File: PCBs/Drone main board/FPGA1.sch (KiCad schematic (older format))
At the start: 1 part, among them U1201 10CL040_F484

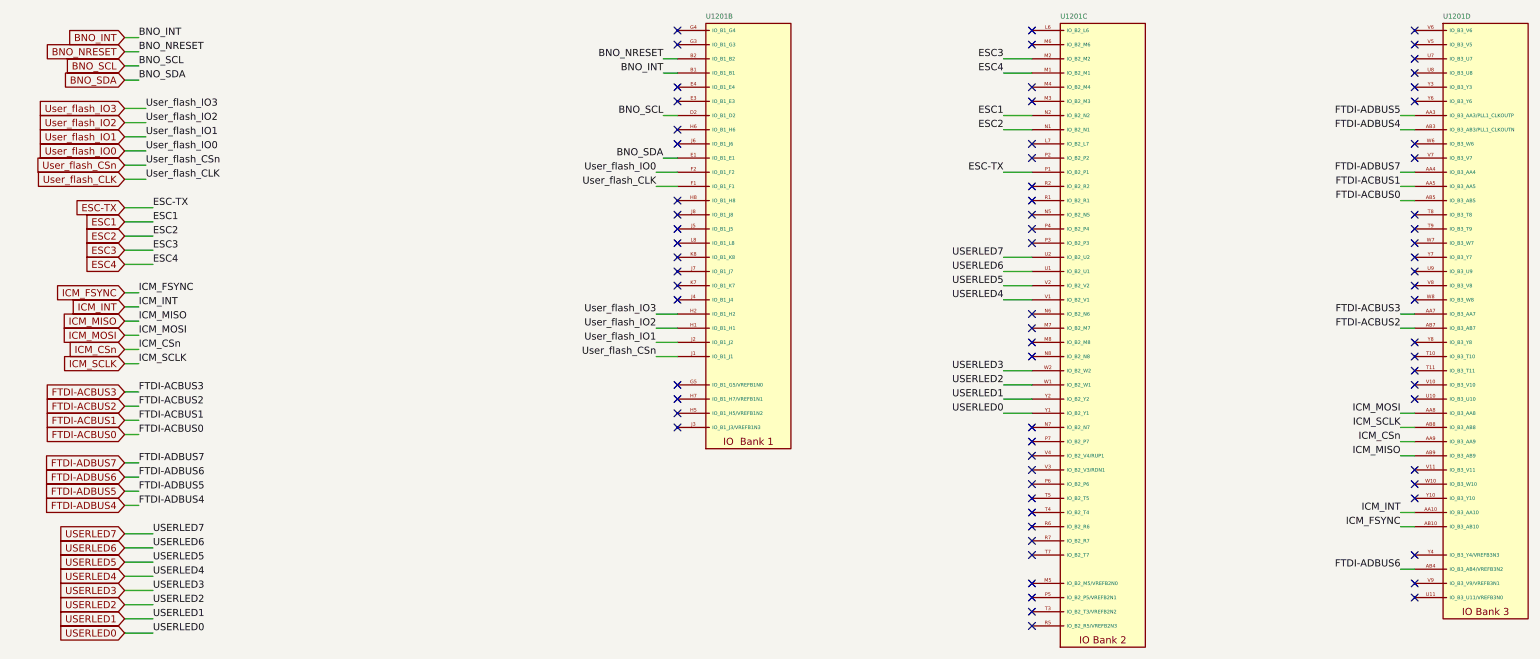
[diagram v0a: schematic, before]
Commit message: Finished (?) the schematic check and update. Next: PCB update
Signed-off-by: Eldalote.Electronics <Eldalote.Electronics@gmail.com>
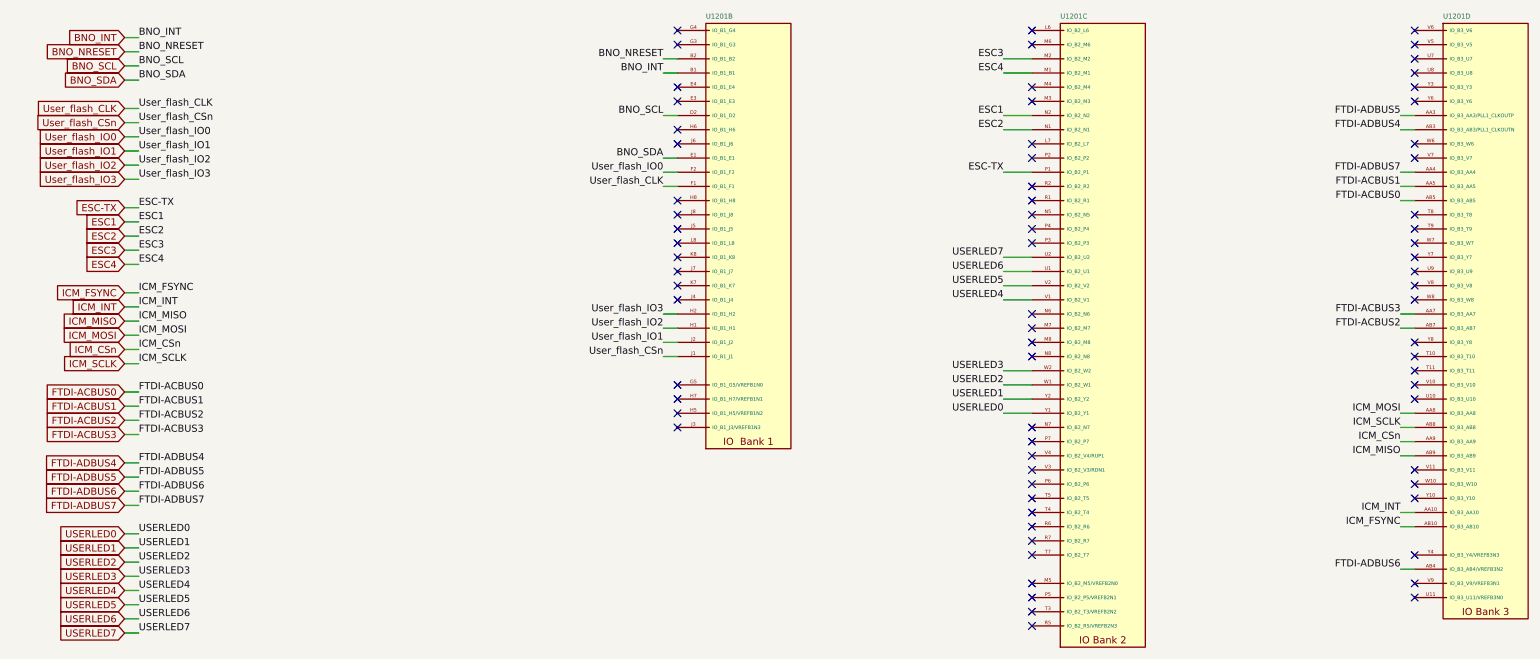
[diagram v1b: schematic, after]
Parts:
- U1201: MfNr (none) -> 10CL040Y
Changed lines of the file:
@@
 F 4 "TRUE" H 6350 -5365 35  0001 L CNN "SPLIT_INST"
 F 5 "(S1+S2+S3+S4+S5+S6+S7+S8+S9+S10+S11+S12+S13)" H 6350 -5410 35  0001 L CNN "SWAP_INFO"
+F 6 "10CL040Y" H 5300 650 50  0001 C CNN "MfNr"
 	2    5300 650
 	1    0    0    -1
@@
 F 4 "TRUE" H 8850 -5365 35  0001 L CNN "SPLIT_INST"
 F 5 "(S1+S2+S3+S4+S5+S6+S7+S8+S9+S10+S11+S12+S13)" H 8850 -5410 35  0001 L CNN "SWAP_INFO"
+F 6 "10CL040Y" H 7800 650 50  0001 C CNN "MfNr"
 	3    7800 650
 	1    0    0    -1
@@
 F 4 "TRUE" H 11550 -5365 35  0001 L CNN "SPLIT_INST"
 F 5 "(S1+S2+S3+S4+S5+S6+S7+S8+S9+S10+S11+S12+S13)" H 11550 -5410 35  0001 L CNN "SWAP_INFO"
+F 6 "10CL040Y" H 10500 650 50  0001 C CNN "MfNr"
 	4    10500 650
 	1    0    0    -1
@@
 Text Label 5000 1000 2    50   ~ 0
 BNO_INT
-Text Label 4950 3000 2    50   ~ 0
+Text Label 5000 3000 2    50   ~ 0
 User_flash_CSn
-Text Label 4950 1700 2    50   ~ 0
+Text Label 5000 1700 2    50   ~ 0
 User_flash_IO0
-Text Label 4950 2900 2    50   ~ 0
+Text Label 5000 2900 2    50   ~ 0
 User_flash_IO1
-Text Label 4950 2800 2    50   ~ 0
+Text Label 5000 2800 2    50   ~ 0
 User_flash_IO2
-Text Label 4950 2700 2    50   ~ 0
+Text Label 5000 2700 2    50   ~ 0
 User_flash_IO3
-Text Label 4950 1800 2    50   ~ 0
+Text Label 5000 1800 2    50   ~ 0
 User_flash_CLK
 Wire Wire Line
-	5100 1800 4950 1800
-Wire Wire Line
-	5100 3000 4950 3000
-Wire Wire Line
-	5100 1700 4950 1700
-Wire Wire Line
-	5100 2900 4950 2900
-Wire Wire Line
-	5100 2800 4950 2800
-Wire Wire Line
-	5100 2700 4950 2700
-Text Label 1350 1650 0    50   ~ 0
+	5100 1800 5000 1800
+Wire Wire Line
+	5100 3000 5000 3000
+Wire Wire Line
+	5100 1700 5000 1700
+Wire Wire Line
+	5100 2900 5000 2900
+Wire Wire Line
+	5100 2800 5000 2800
+Wire Wire Line
+	5100 2700 5000 2700
+Text Label 1300 1350 0    50   ~ 0
 User_flash_CSn
-Text Label 1350 1550 0    50   ~ 0
+Text Label 1300 1450 0    50   ~ 0
 User_flash_IO0
-Text Label 1350 1450 0    50   ~ 0
+Text Label 1300 1550 0    50   ~ 0
 User_flash_IO1
-Text Label 1350 1350 0    50   ~ 0
+Text Label 1300 1650 0    50   ~ 0
 User_flash_IO2
-Text Label 1350 1250 0    50   ~ 0
+Text Label 1300 1750 0    50   ~ 0
 User_flash_IO3
-Text Label 1350 1750 0    50   ~ 0
+Text Label 1300 1250 0    50   ~ 0
 User_flash_CLK
+Text GLabel 1200 1250 0    50   Input ~ 0
+User_flash_CLK
+Text GLabel 1200 1350 0    50   Input ~ 0
+User_flash_CSn
+Text GLabel 1200 1450 0    50   Input ~ 0
+User_flash_IO0
+Text GLabel 1200 1550 0    50   Input ~ 0
+User_flash_IO1
+Text GLabel 1200 1650 0    50   Input ~ 0
+User_flash_IO2
 Text GLabel 1200 1750 0    50   Input ~ 0
-User_flash_CLK
-Text GLabel 1200 1650 0    50   Input ~ 0
-User_flash_CSn
-Text GLabel 1200 1550 0    50   Input ~ 0
-User_flash_IO0
-Text GLabel 1200 1450 0    50   Input ~ 0
-User_flash_IO1
-Text GLabel 1200 1350 0    50   Input ~ 0
-User_flash_IO2
-Text GLabel 1200 1250 0    50   Input ~ 0
 User_flash_IO3
 Wire Wire Line
-	1200 1750 1350 1750
-Wire Wire Line
-	1200 1650 1350 1650
-Wire Wire Line
-	1200 1550 1350 1550
-Wire Wire Line
-	1200 1450 1350 1450
-Wire Wire Line
-	1200 1350 1350 1350
-Wire Wire Line
-	1200 1250 1350 1250
+	1200 1250 1300 1250
+Wire Wire Line
+	1200 1350 1300 1350
+Wire Wire Line
+	1200 1450 1300 1450
+Wire Wire Line
+	1200 1550 1300 1550
+Wire Wire Line
+	1200 1650 1300 1650
+Wire Wire Line
+	1200 1750 1300 1750
 Text GLabel 1200 2350 0    50   Input ~ 0
 ESC4
@@
 ESC-TX
 Wire Wire Line
-	1200 1950 1400 1950
-Text Label 1400 1950 0    50   ~ 0
+	1200 1950 1300 1950
+Text Label 1300 1950 0    50   ~ 0
 ESC-TX
-Text Label 1400 2050 0    50   ~ 0
+Text Label 1300 2050 0    50   ~ 0
 ESC1
-Text Label 1400 2150 0    50   ~ 0
+Text Label 1300 2150 0    50   ~ 0
 ESC2
-Text Label 1400 2250 0    50   ~ 0
+Text Label 1300 2250 0    50   ~ 0
 ESC3
-Text Label 1400 2350 0    50   ~ 0
+Text Label 1300 2350 0    50   ~ 0
 ESC4
 Wire Wire Line
-	1200 2050 1400 2050
-Wire Wire Line
-	1200 2150 1400 2150
-Wire Wire Line
-	1200 2250 1400 2250
-Wire Wire Line
-	1200 2350 1400 2350
+	1200 2050 1300 2050
+Wire Wire Line
+	1200 2150 1300 2150
+Wire Wire Line
+	1200 2250 1300 2250
+Wire Wire Line
+	1200 2350 1300 2350
 Wire Wire Line
 	7600 1700 7400 1700
@@
 Text Label 10200 4200 2    50   ~ 0
 ICM_FSYNC
+Text Label 1300 3750 0    50   ~ 0
+FTDI-ADBUS4
+Text Label 1300 3850 0    50   ~ 0
+FTDI-ADBUS5
+Text Label 1300 3950 0    50   ~ 0
+FTDI-ADBUS6
 Text Label 1300 4050 0    50   ~ 0
+FTDI-ADBUS7
+Text Label 1300 3250 0    50   ~ 0
+FTDI-ACBUS0
+Text Label 1300 3350 0    50   ~ 0
+FTDI-ACBUS1
+Text Label 1300 3450 0    50   ~ 0
+FTDI-ACBUS2
+Text Label 1300 3550 0    50   ~ 0
+FTDI-ACBUS3
+Wire Wire Line
+	1300 3750 1200 3750
+Wire Wire Line
+	1300 3850 1200 3850
+Wire Wire Line
+	1300 3950 1200 3950
+Wire Wire Line
+	1300 4050 1200 4050
+Wire Wire Line
+	1300 3250 1200 3250
+Wire Wire Line
+	1300 3350 1200 3350
+Wire Wire Line
+	1300 3450 1200 3450
+Wire Wire Line
+	1300 3550 1200 3550
+Text GLabel 1200 3750 0    50   Input ~ 0
 FTDI-ADBUS4
-Text Label 1300 3950 0    50   ~ 0
+Text GLabel 1200 3850 0    50   Input ~ 0
 FTDI-ADBUS5
-Text Label 1300 3850 0    50   ~ 0
+Text GLabel 1200 3950 0    50   Input ~ 0
 FTDI-ADBUS6
-Text Label 1300 3750 0    50   ~ 0
+Text GLabel 1200 4050 0    50   Input ~ 0
 FTDI-ADBUS7
-Text Label 1300 3550 0    50   ~ 0
+Text GLabel 1200 3250 0    50   Input ~ 0
 FTDI-ACBUS0
-Text Label 1300 3450 0    50   ~ 0
+Text GLabel 1200 3350 0    50   Input ~ 0
 FTDI-ACBUS1
-Text Label 1300 3350 0    50   ~ 0
+Text GLabel 1200 3450 0    50   Input ~ 0
 FTDI-ACBUS2
-Text Label 1300 3250 0    50   ~ 0
-FTDI-ACBUS3
-Wire Wire Line
-	1300 4050 1200 4050
-Wire Wire Line
-	1300 3950 1200 3950
-Wire Wire Line
-	1300 3850 1200 3850
-Wire Wire Line
-	1300 3750 1200 3750
-Wire Wire Line
-	1300 3550 1200 3550
-Wire Wire Line
-	1300 3450 1200 3450
-Wire Wire Line
-	1300 3350 1200 3350
-Wire Wire Line
-	1300 3250 1200 3250
-Text GLabel 1200 4050 0    50   Input ~ 0
-FTDI-ADBUS4
-Text GLabel 1200 3950 0    50   Input ~ 0
-FTDI-ADBUS5
-Text GLabel 1200 3850 0    50   Input ~ 0
-FTDI-ADBUS6
-Text GLabel 1200 3750 0    50   Input ~ 0
-FTDI-ADBUS7
 Text GLabel 1200 3550 0    50   Input ~ 0
-FTDI-ACBUS0
-Text GLabel 1200 3450 0    50   Input ~ 0
-FTDI-ACBUS1
-Text GLabel 1200 3350 0    50   Input ~ 0
-FTDI-ACBUS2
-Text GLabel 1200 3250 0    50   Input ~ 0
 FTDI-ACBUS3
 Text Label 10200 1400 2    50   ~ 0
@@
 	10200 2700 10300 2700
 Wire Wire Line
-	1400 4950 1200 4950
-Wire Wire Line
-	1400 4850 1200 4850
-Wire Wire Line
-	1400 4750 1200 4750
-Wire Wire Line
-	1400 4650 1200 4650
-Wire Wire Line
-	1400 4550 1200 4550
-Wire Wire Line
-	1400 4450 1200 4450
-Wire Wire Line
-	1400 4350 1200 4350
-Wire Wire Line
-	1400 4250 1200 4250
-Text Label 1400 4950 0    50   ~ 0
+	1300 4250 1200 4250
+Wire Wire Line
+	1300 4350 1200 4350
+Wire Wire Line
+	1300 4450 1200 4450
+Wire Wire Line
+	1300 4550 1200 4550
+Wire Wire Line
+	1300 4650 1200 4650
+Wire Wire Line
+	1300 4750 1200 4750
+Wire Wire Line
+	1300 4850 1200 4850
+Wire Wire Line
+	1300 4950 1200 4950
+Text Label 1300 4250 0    50   ~ 0
 USERLED0
-Text Label 1400 4850 0    50   ~ 0
+Text Label 1300 4350 0    50   ~ 0
 USERLED1
-Text Label 1400 4750 0    50   ~ 0
+Text Label 1300 4450 0    50   ~ 0
 USERLED2
-Text Label 1400 4650 0    50   ~ 0
+Text Label 1300 4550 0    50   ~ 0
 USERLED3
-Text Label 1400 4550 0    50   ~ 0
+Text Label 1300 4650 0    50   ~ 0
 USERLED4
-Text Label 1400 4450 0    50   ~ 0
+Text Label 1300 4750 0    50   ~ 0
 USERLED5
-Text Label 1400 4350 0    50   ~ 0
+Text Label 1300 4850 0    50   ~ 0
 USERLED6
-Text Label 1400 4250 0    50   ~ 0
+Text Label 1300 4950 0    50   ~ 0
 USERLED7
+Text GLabel 1200 4250 0    50   Input ~ 0
+USERLED0
+Text GLabel 1200 4350 0    50   Input ~ 0
+USERLED1
+Text GLabel 1200 4450 0    50   Input ~ 0
+USERLED2
+Text GLabel 1200 4550 0    50   Input ~ 0
+USERLED3
+Text GLabel 1200 4650 0    50   Input ~ 0
+USERLED4
+Text GLabel 1200 4750 0    50   Input ~ 0
+USERLED5
+Text GLabel 1200 4850 0    50   Input ~ 0
+USERLED6
 Text GLabel 1200 4950 0    50   Input ~ 0
-USERLED0
-Text GLabel 1200 4850 0    50   Input ~ 0
-USERLED1
-Text GLabel 1200 4750 0    50   Input ~ 0
-USERLED2
-Text GLabel 1200 4650 0    50   Input ~ 0
-USERLED3
-Text GLabel 1200 4550 0    50   Input ~ 0
-USERLED4
-Text GLabel 1200 4450 0    50   Input ~ 0
-USERLED5
-Text GLabel 1200 4350 0    50   Input ~ 0
-USERLED6
-Text GLabel 1200 4250 0    50   Input ~ 0
 USERLED7
 Wire Wire Line
